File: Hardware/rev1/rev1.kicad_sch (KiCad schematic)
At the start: 0 parts

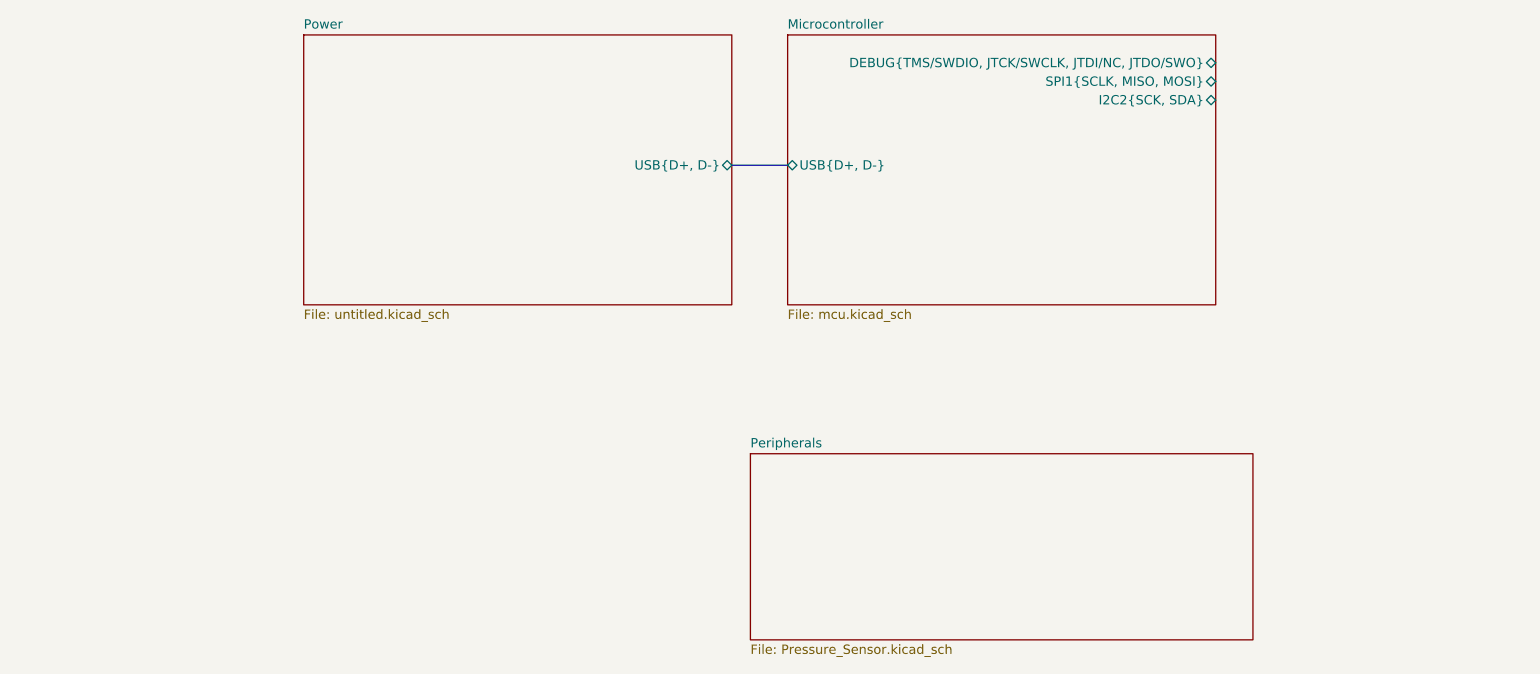
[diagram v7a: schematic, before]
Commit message: Removed backup files and folder as redundant on GitHub, updated hierarchical labels to include NRESET
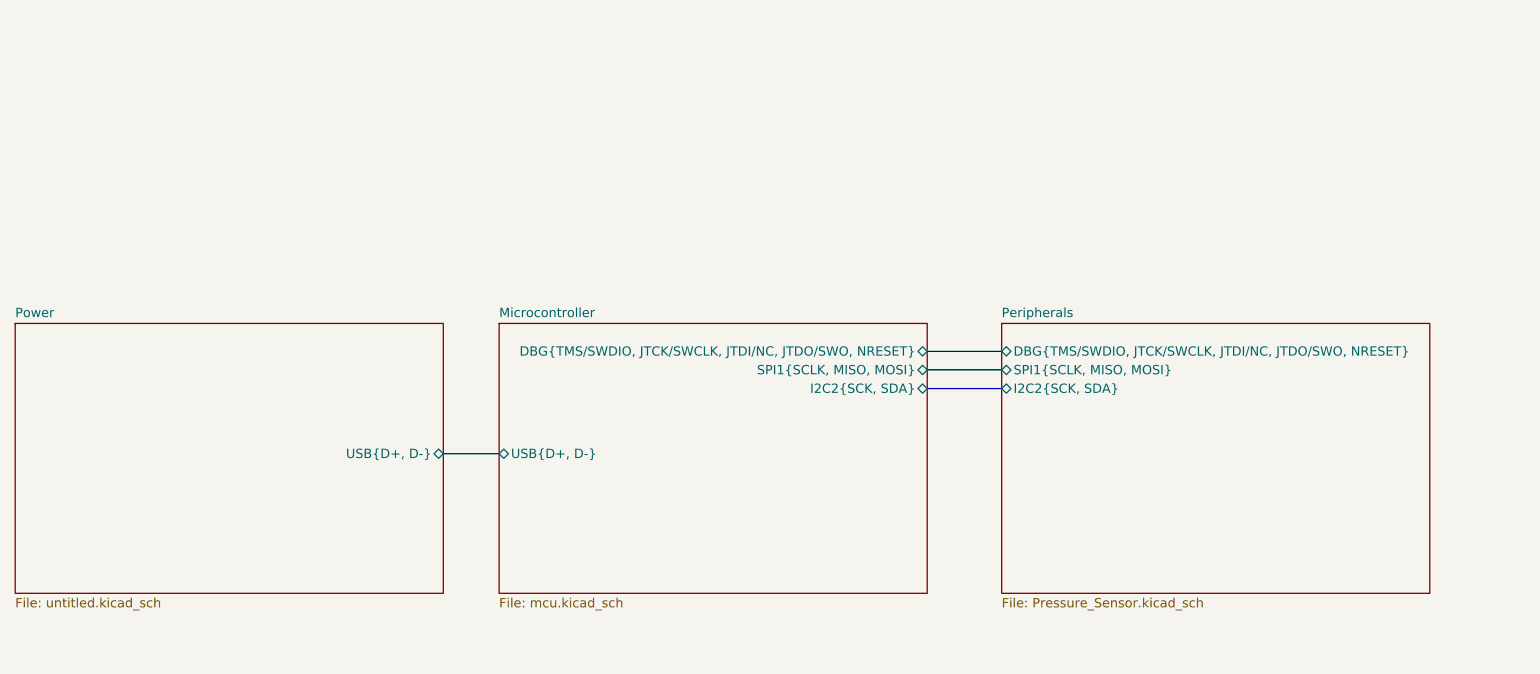
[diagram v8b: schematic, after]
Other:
- sheet Microcontroller ports: added DBG{TMS/SWDIO, JTCK/SWCLK, JTDI/NC, JTDO/SWO, NRESET}; removed DEBUG{TMS/SWDIO, JTCK/SWCLK, JTDI/NC, JTDO/SWO}
- sheet Peripherals ports: added DBG{TMS/SWDIO, JTCK/SWCLK, JTDI/NC, JTDO/SWO, NRESET}, I2C2{SCK, SDA}, SPI1{SCLK, MISO, MOSI}; removed none
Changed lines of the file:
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@@
 	(bus
 		(pts
-			(xy 143.51 57.15) (xy 151.13 57.15)
+			(xy 170.18 85.09) (xy 180.34 85.09)
+		)
+		(stroke
+			(width 0)
+			(type default)
+		)
+	)
+	(bus
+		(pts
+			(xy 170.18 82.55) (xy 180.34 82.55)
+		)
+		(stroke
+			(width 0)
+			(type default)
+		)
+	)
+	(bus
+		(pts
+			(xy 104.14 96.52) (xy 111.76 96.52)
+		)
+		(stroke
+			(width 0)
+			(type default)
+		)
+	)
+	(bus
+		(pts
+			(xy 170.18 87.63) (xy 180.34 87.63)
 		)
 		(stroke
@@
 	)
 	(sheet
-		(at 151.13 39.37)
+		(at 111.76 78.74)
 		(size 58.42 36.83)
 		(fields_autoplaced yes)
@@
 		)
 		(property "Sheetname" "Microcontroller"
-			(at 151.13 38.6584 0)
+			(at 111.76 78.0284 0)
 			(effects
 				(font
@@
 		)
 		(property "Sheetfile" "mcu.kicad_sch"
-			(at 151.13 76.7846 0)
+			(at 111.76 116.1546 0)
 			(effects
 				(font
@@
 		)
 		(pin "USB{D+, D-}" bidirectional
-			(at 151.13 57.15 180)
-			(effects
-				(font
-					(size 1.27 1.27)
-				)
-				(justify left)
-			)
-		)
-		(pin "DEBUG{TMS{slash}SWDIO, JTCK{slash}SWCLK, JTDI{slash}NC, JTDO{slash}SWO}"
+			(at 111.76 96.52 180)
+			(effects
+				(font
+					(size 1.27 1.27)
+				)
+				(justify left)
+			)
+		)
+		(pin "DBG{TMS{slash}SWDIO, JTCK{slash}SWCLK, JTDI{slash}NC, JTDO{slash}SWO, NRESET}"
 			bidirectional
-			(at 209.55 43.18 0
+			(at 170.18 82.55 0
 			)
 			(effects
@@
 		)
 		(pin "SPI1{SCLK, MISO, MOSI}" bidirectional
-			(at 209.55 45.72 0)
+			(at 170.18 85.09 0)
 			(effects
 				(font
@@
 		)
 		(pin "I2C2{SCK, SDA}" bidirectional
-			(at 209.55 48.26 0)
+			(at 170.18 87.63 0)
 			(effects
 				(font
@@
 	)
 	(sheet
-		(at 85.09 39.37)
+		(at 45.72 78.74)
 		(size 58.42 36.83)
 		(fields_autoplaced yes)
@@
 		)
 		(property "Sheetname" "Power"
-			(at 85.09 38.6584 0)
+			(at 45.72 78.0284 0)
 			(effects
 				(font
@@
 		)
 		(property "Sheetfile" "untitled.kicad_sch"
-			(at 85.09 76.7846 0)
+			(at 45.72 116.1546 0)
 			(effects
 				(font
@@
 		)
 		(pin "USB{D+, D-}" bidirectional
-			(at 143.51 57.15 0)
+			(at 104.14 96.52 0)
 			(effects
 				(font
@@
 	)
 	(sheet
-		(at 146.05 96.52)
-		(size 68.58 25.4)
+		(at 180.34 78.74)
+		(size 58.42 36.83)
 		(fields_autoplaced yes)
 		(stroke
@@
 		)
 		(property "Sheetname" "Peripherals"
-			(at 146.05 95.8084 0)
+			(at 180.34 78.0284 0)
 			(effects
 				(font
@@
 		)
 		(property "Sheetfile" "Pressure_Sensor.kicad_sch"
-			(at 146.05 122.5046 0)
+			(at 180.34 116.1546 0)
 			(effects
 				(font
@@
 		)
 		(property "Field2" ""
-			(at 146.05 96.52 0)
+			(at 180.34 78.74 0)
 			(effects
 				(font
@@
 			)
 		)
+		(pin "I2C2{SCK, SDA}" bidirectional
+			(at 180.34 87.63 180)
+			(effects
+				(font
+					(size 1.27 1.27)
+				)
+				(justify left)
+			)
+		)
+		(pin "DBG{TMS{slash}SWDIO, JTCK{slash}SWCLK, JTDI{slash}NC, JTDO{slash}SWO, NRESET}"
+			bidirectional
+			(at 180.34 82.55 180
+			)
+			(effects
+				(font
+					(size 1.27 1.27)
+				)
+				(justify left)
+			)
+		)
+		(pin "SPI1{SCLK, MISO, MOSI}" bidirectional
+			(at 180.34 85.09 180)
+			(effects
+				(font
+					(size 1.27 1.27)
+				)
+				(justify left)
+			)
+		)
